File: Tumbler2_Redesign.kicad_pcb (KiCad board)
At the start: 2 copper layers, 77 x 84 mm, 93 parts, among them J1 Conn_01x02, J2 Conn_01x10, J3 Conn_01x10, J4 USB_C_Receptacle_USB2.0_16P, J5 Conn_01x04, J6 Conn_01x06, J7 Conn_01x06, SW1 SW_Push, SW2 SW_Push, SW3 SW_Push, U1 AMS1117-5.0, U2 AP63203WU, U3 ESP32-S3-WROOM-1, U4 USBLC6-2SC6, U5 LSM6DSV, U6 TB67H450FNG_EL, U7 TB67H450FNG_EL

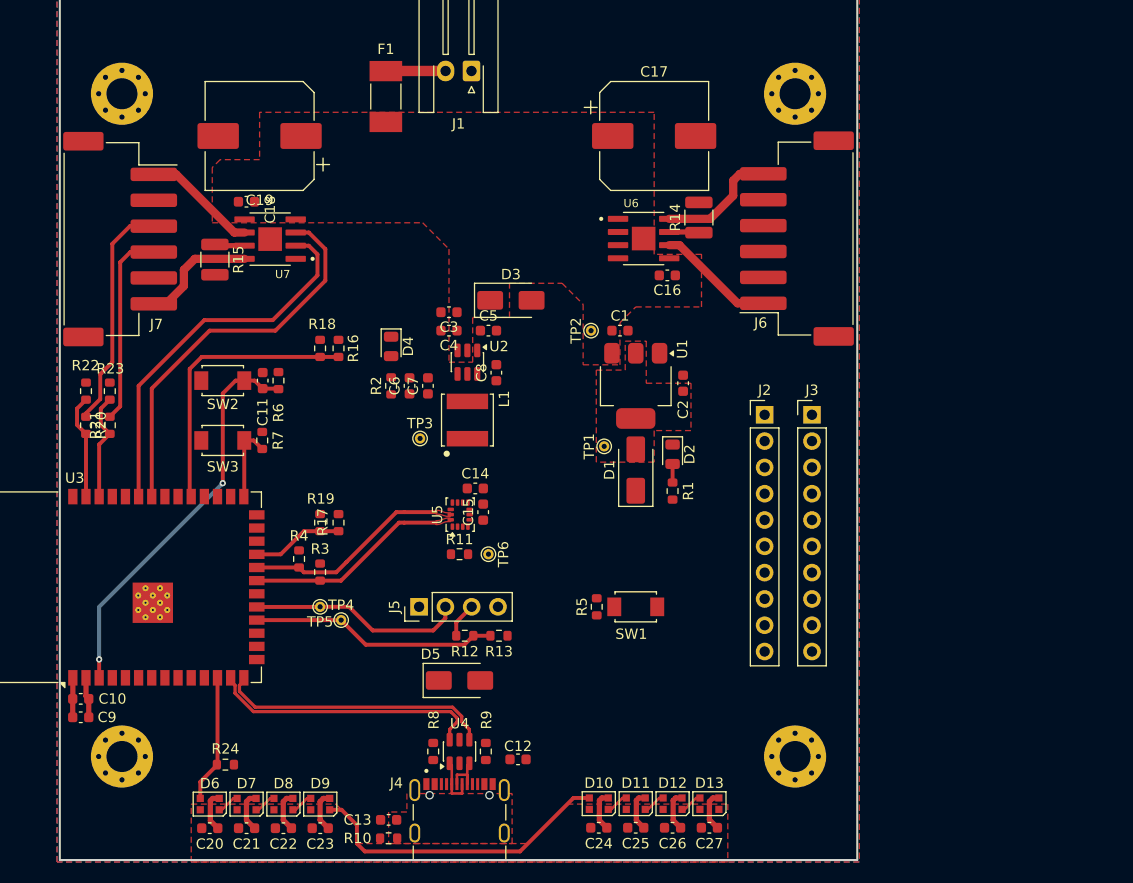
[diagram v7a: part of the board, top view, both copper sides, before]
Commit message: Continue layout and add pin header protection
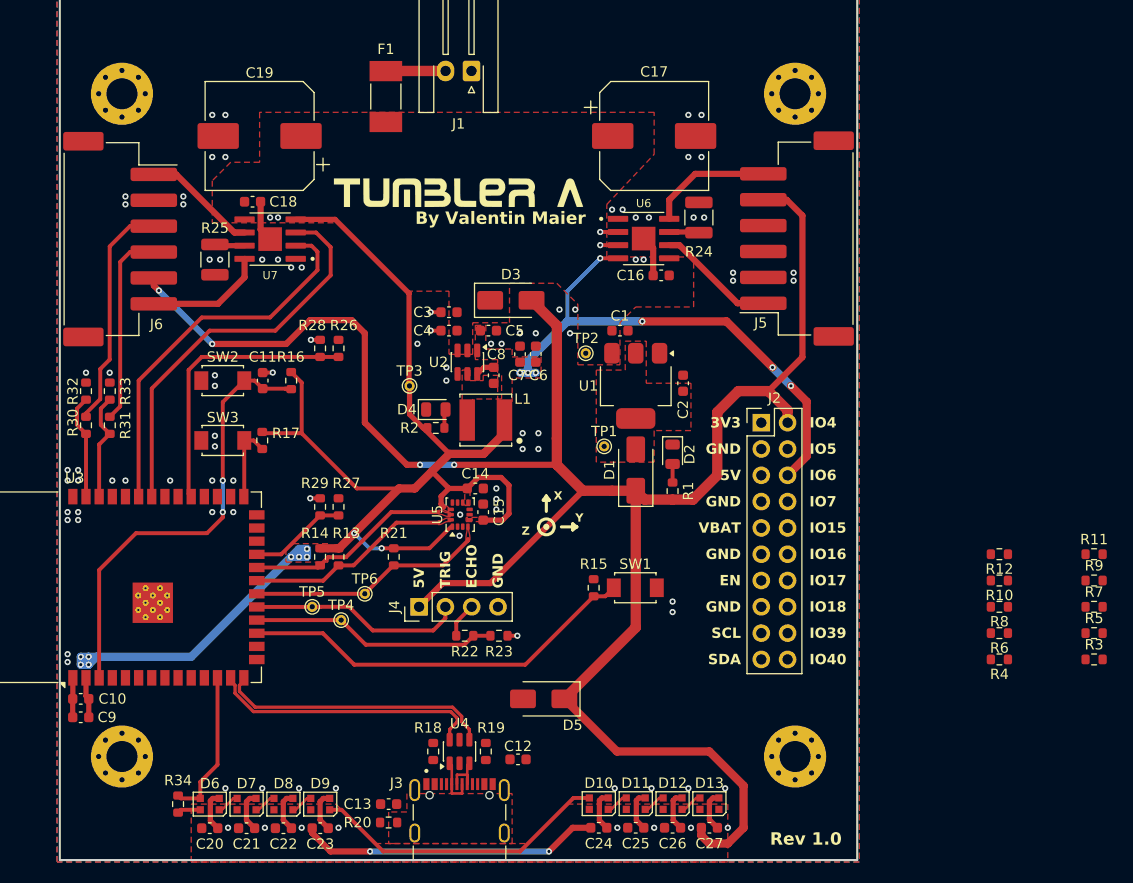
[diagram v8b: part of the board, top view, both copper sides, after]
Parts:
- removed the J3 at (186.4, 102.4)
- added G***: LOGO, Tumbler2:Tumbler2_Title, F.Cu at (152.4, 80.8)
- added R10: 100, Resistor_SMD:R_0603_1608Metric, F.Cu at (204.5, 118.4)
- added R11: 100, Resistor_SMD:R_0603_1608Metric, F.Cu at (213.7, 115.8)
- added R12: 100, Resistor_SMD:R_0603_1608Metric, F.Cu at (204.5, 115.8)
- added R3: 100, Resistor_SMD:R_0603_1608Metric, F.Cu at (213.7, 126.0)
- added R4: 100, Resistor_SMD:R_0603_1608Metric, F.Cu at (204.5, 126.0)
- added R5: 100, Resistor_SMD:R_0603_1608Metric, F.Cu at (213.7, 123.4)
- added R6: 100, Resistor_SMD:R_0603_1608Metric, F.Cu at (204.5, 123.4)
- added R7: 100, Resistor_SMD:R_0603_1608Metric, F.Cu at (213.7, 120.9)
- added R8: 100, Resistor_SMD:R_0603_1608Metric, F.Cu at (204.5, 120.9)
- added R9: 100, Resistor_SMD:R_0603_1608Metric, F.Cu at (213.7, 118.4)
- J2: value Conn_01x10 -> Conn_02x10_Counter_Clockwise; footprint Connector_PinHeader_2.54mm:PinHeader_1x10_P2.54mm_Vertical -> Connector_PinHeader_2.54mm:PinHeader_2x10_P2.54mm_Vertical
- moved C6 12.6 mm to (159.8, 96.5)
- moved TP6 12.5 mm to (143.3, 119.6), turned to 0 degrees
- moved C7 9.40 mm to (158.2, 96.5)
- moved D5 8.32 mm to (160.5, 129.8), turned to 180 degrees
- moved D4 7.47 mm to (150.1, 101.9), turned to 0 degrees
- moved R21 6.36 mm to (146.1, 116.1), turned to -90 degrees
- moved R34 5.95 mm to (125.2, 140.0), turned to 90 degrees
- moved R2 5.93 mm to (150.1, 103.6), turned to 0 degrees
- moved TP3 5.18 mm to (147.6, 99.6)
- moved R13 2.31 mm to (140.7, 116.1)
- moved TP2 2.24 mm to (164.6, 96.4), turned to 0 degrees
- moved R14 2.04 mm to (138.9, 116.1)
- moved R15 1.86 mm to (165.4, 119.1), turned to -90 degrees
- moved SW1 1.84 mm to (169.4, 119.1)
- moved L1 1.78 mm to (154.9, 102.9), turned to 180 degrees
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- renumbered J4 to J3, J5 to J4, J6 to J5, J7 to J6, R3 to R13, R4 to R14, R5 to R15, R6 to R16, R7 to R17, R8 to R18, R9 to R19, R10 to R20, R11 to R21, R12 to R22, R13 to R23, R14 to R24, R15 to R25, R16 to R26, R17 to R27, R18 to R28, R19 to R29, R20 to R30, R21 to R31, R22 to R32, R23 to R33, R24 to R34
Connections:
- J2 pad 1: GND -> Net-(J2-Pin_1)
- J2 pad 10: GND -> VBAT
- J2 pad 2: 3.3V -> 5V
- J2 pad 3: 3.3V -> Net-(J2-Pin_3)
- J2 pad 5: 5V -> Net-(J2-Pin_5)
- J2 pad 6: 5V -> 3.3V
- J2 pad 7: GND -> Net-(J2-Pin_7)
- J2 pad 8: VBAT -> GND
- J2 pad 9: VBAT -> Net-(J2-Pin_9)
- U3 pad 10: unconnected-(U3-IO17-Pad10) -> /MCU/IO17
- U3 pad 11: unconnected-(U3-IO18-Pad11) -> /MCU/IO18
- U3 pad 20: /MCU/IO12 -> /MCU/INT1
- U3 pad 32: unconnected-(U3-IO39-Pad32) -> /MCU/IO39
- U3 pad 33: unconnected-(U3-IO40-Pad33) -> /MCU/IO40
- U3 pad 4: /MCU/IO9 -> /MCU/IO4
- U3 pad 5: /MCU/INT1 -> /MCU/IO5
- U3 pad 6: /MCU/IO10 -> /MCU/IO6
- U3 pad 7: /MCU/IO11 -> /MCU/IO7
- U3 pad 8: unconnected-(U3-IO15-Pad8) -> /MCU/IO15
- U3 pad 9: unconnected-(U3-IO16-Pad9) -> /MCU/IO16
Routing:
- net 5V: track 0.00 -> 232.3 mm, vias 0 -> 6
- net 3.3V: track 3.92 -> 194.5 mm, vias 0 -> 17
- net /MCU/BTN: track 0.00 -> 38.8 mm
- net /MCU/INT1: track 0.00 -> 22.7 mm
- net GND: track 35.2 -> 48.9 mm, vias 0 -> 98
- net /MCU/ENABLE: track 38.6 -> 43.4 mm
- net /MCU/RGB: track 12.3 -> 14.6 mm
- net Net-(U2-BST): track 0.00 -> 1.86 mm
- net Net-(D4-A): track 0.00 -> 1.82 mm
- net /MCU/AIN2: track 0.00 -> 1.72 mm, vias 0 -> 1
- net /MCU/AIN1: track 0.00 -> 1.72 mm, vias 0 -> 1
- net Net-(D10-DIN): track 29.9 -> 28.9 mm
- net /MCU/BIN1: track 38.1 -> 38.9 mm
- net /MCU/ENCA_A: track 8.82 -> 9.45 mm
- added copper zone on F.Cu, net /MCU/INT1
- added copper zone on F.Cu, net 3.3V
- added copper zone on F.Cu, net Net-(U2-SW)
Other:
- board text added: "3V3"
- board text added: "5V"
- board text added: "By Valentin Maier"
- board text added: "ECHO"
- board text added: "EN"
- board text added: "GND"
- board text added: "IO15"
- board text added: "IO16"
- board text added: "IO17"
- board text added: "IO18"
- board text added: "IO39"
- board text added: "IO4"
- board text added: "IO40"
- board text added: "IO5"
- board text added: "IO6"
- board text added: "IO7"
- board text added: "Rev 1.0"
- board text added: "SCL"
- board text added: "SDA"
- board text added: "TRIG"
- board text added: "VBAT"
- board text added: "X"
- board text added: "Y"
- board text added: "Z"
